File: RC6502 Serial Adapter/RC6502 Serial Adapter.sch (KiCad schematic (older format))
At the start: 27 parts, among them J1 FTDI, J2 RS232, J3 Port, J4 Base, J5 RC6502_Backplane, J6 IRQ_SEL, U1 R6551, U3 MAX232, U4 74LS138, U5 74LS138, X1 TCXO-14, Y1 1.8432Mhz

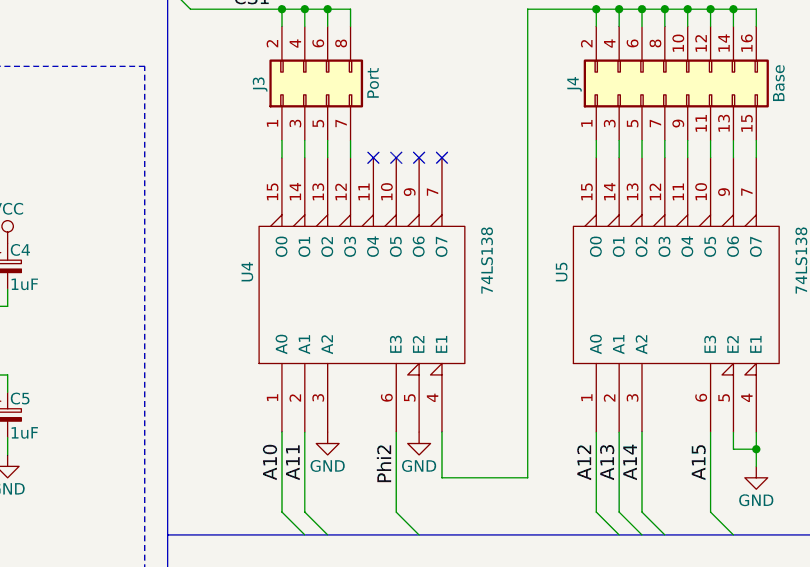
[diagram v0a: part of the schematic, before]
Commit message: SBC board cleaned up and exported
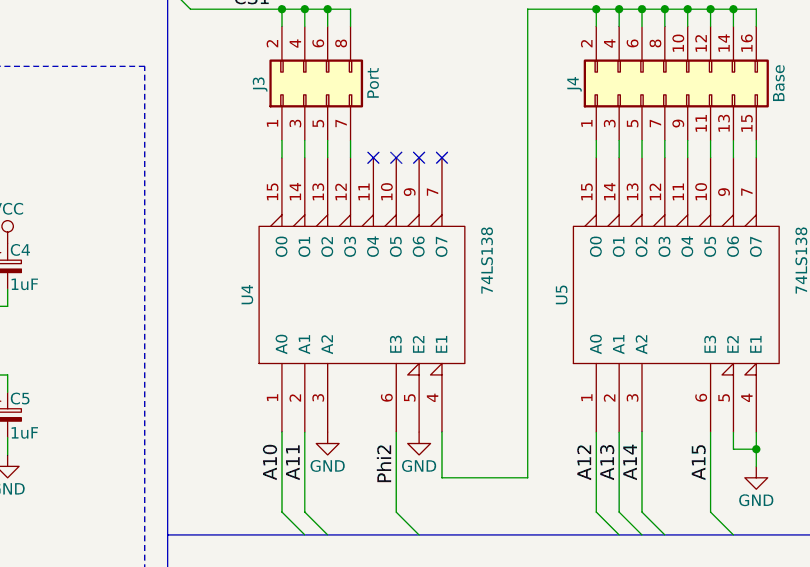
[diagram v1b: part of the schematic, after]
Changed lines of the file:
@@
 U 1 1 5C3F2CED
 P 8100 2200
-F 0 "U5" H 8200 2700 50  0000 C CNN
+F 0 "U5" H 8100 2700 50  0000 C CNN
 F 1 "74LS138" H 8250 1651 50  0000 C CNN
 F 2 "Housings_DIP:DIP-16_W7.62mm" H 8100 2200 50  0001 C CNN
@@
 U 1 1 5C3F2CEE
 P 6725 2200
-F 0 "U4" H 6825 2700 50  0000 C CNN
+F 0 "U4" H 6725 2700 50  0000 C CNN
 F 1 "74LS138" H 6875 1651 50  0000 C CNN
 F 2 "Housings_DIP:DIP-16_W7.62mm" H 6725 2200 50  0001 C CNN
